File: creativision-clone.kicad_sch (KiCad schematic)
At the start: 0 parts

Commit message: ROM wired up
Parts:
- added C1: 1µF, symbol Device:C_Small
- added JP1, JP2, JP3, JP4: SolderJumper_2_Bridged, symbol Jumper:SolderJumper_2_Bridged
- added R1: 3.3kΩ, symbol Device:R_Small_US
- added R66: 47kΩ, symbol Device:R_Small_US
- added SW1: Reset, symbol Switch:SW_Push
- added U1: 6821, Package_DIP:DIP-40_W15.24mm, symbol Interface:6821
- added U2: SN76489AN, symbol LeakoChips:SN76489AN
- added U3: 6502, Package_DIP:DIP-40_W15.24mm, symbol 65xx:6502
- added U4: TMS9918A, Housings_DIP:DIP-40_W15.24mm_Socket_LongPads, symbol LeakoChips:TMS9918A
- added U5: 27256, Package_DIP:DIP-28_W15.24mm, symbol Memory_EPROM:27256
- added X1: 2MHz, Oscillator:Oscillator_DIP-8, symbol Oscillator:CXO_DIP8
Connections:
- new net: R1.2, SW1.2, U3.6 (~{NMI})
- new net: JP2.2 (B), U5.2 (A12)
- new net: JP1.2 (B), U5.23 (A11)
- new net: JP3.2 (B), U5.26 (A13)
- new net: JP4.2 (B), U5.27 (A14)
- new net +5V: R1.1, R66.1, U3.8 (VCC), U5.28 (VCC), X1.1 (EN), X1.8 (Vcc)
- new net CPUCLK: U3.37 (ϕ0), X1.5 (OUT)
- new net GND: C1.2, JP1.1 (A), JP2.1 (A), JP3.1 (A), JP4.1 (A), SW1.1, U3.1 (VSS), U3.21 (VSS), U5.1 (VPP), U5.14 (GND), X1.4 (GND)
- new net a0: U5.10 (A0)
- new net a1: U5.9 (A1)
- new net a10: U5.21 (A10)
- new net a2: U5.8 (A2)
- new net a3: U5.7 (A3)
- new net a4: U5.6 (A4)
- new net a5: U5.5 (A5)
- new net a6: U5.4 (A6)
- new net a7: U5.3 (A7)
- new net a8: U5.25 (A8)
- new net a9: U5.24 (A9)
- new net d0: U3.33 (D0), U5.11 (D0)
- new net d1: U3.32 (D1), U5.12 (D1)
- new net d2: U3.31 (D2), U5.13 (D2)
- new net d3: U3.30 (D3), U5.15 (D3)
- new net d4: U3.29 (D4), U5.16 (D4)
- new net d5: U3.28 (D5), U5.17 (D5)
- new net d6: U3.27 (D6), U5.18 (D6)
- new net d7: U3.26 (D7), U5.19 (D7)
- new net ~{RESET}: C1.1, R66.2, U3.40 (~{RES})
- new net ~{ROM_RD}: U5.20 (~{CE}), U5.22 (~{OE})
- no-connect marks 0 -> 4
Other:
- note added: "TODO: 9918 interrupt"
- note added: "TODO: 9918 w/r drive"
- note added: "TODO: Which project is it that I had the dual footprint oscillator in?"
- note added: "TODO: are there alternative roms we might want to run?"

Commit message: Work RAM
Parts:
- added R14: 1kΩ, symbol Device:R_Small_US
- added U15: 74LS139, symbol 74xx:74LS139
- added U6: AS6C62256-DIP, Housings_DIP:DIP-28_W15.24mm_Socket_LongPads, symbol AS6C62256:AS6C62256-DIP
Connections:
- net +5V: now also U15.16 (VCC), U6.28 (Vcc)
- net GND: now also U15.15 (E), U15.8 (GND)
- net d0: now also U6.11 (DQ0)
- net d1: now also U6.12 (DQ1)
- net d2: now also U6.13 (DQ2)
- net d3: now also U6.15 (DQ3)
- net d4: now also U6.16 (DQ4)
- net d5: now also U6.17 (DQ5)
- net d6: now also U6.18 (DQ6)
- net d7: now also U6.19 (DQ7)
- new net: R14.2, U6.20 (~{CE})
- new net: U15.1 (E), U15.12 (O0)
- new net: R14.1, U15.4 (O0)
- new net a12: U15.2 (A0)
- new net a13: U15.3 (A1)
- new net a14: U15.14 (A0)
- new net a15: U15.13 (A1)
- new net ~{PIA}: U15.5 (O1)
- new net ~{ROM0}: U15.9 (O3)
- new net ~{ROM1}: U15.10 (O2)
- new net ~{ROM2}: U15.11 (O1)
- new net ~{VDP_R}: U15.6 (O2)
- new net ~{VDP_W}: U15.7 (O3)
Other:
- note added: "BIOS ROM"
- note added: "Main System RAM"
- note added: "TODO: Connector P1?"
- note added: "TODO: R/W W/R signals"

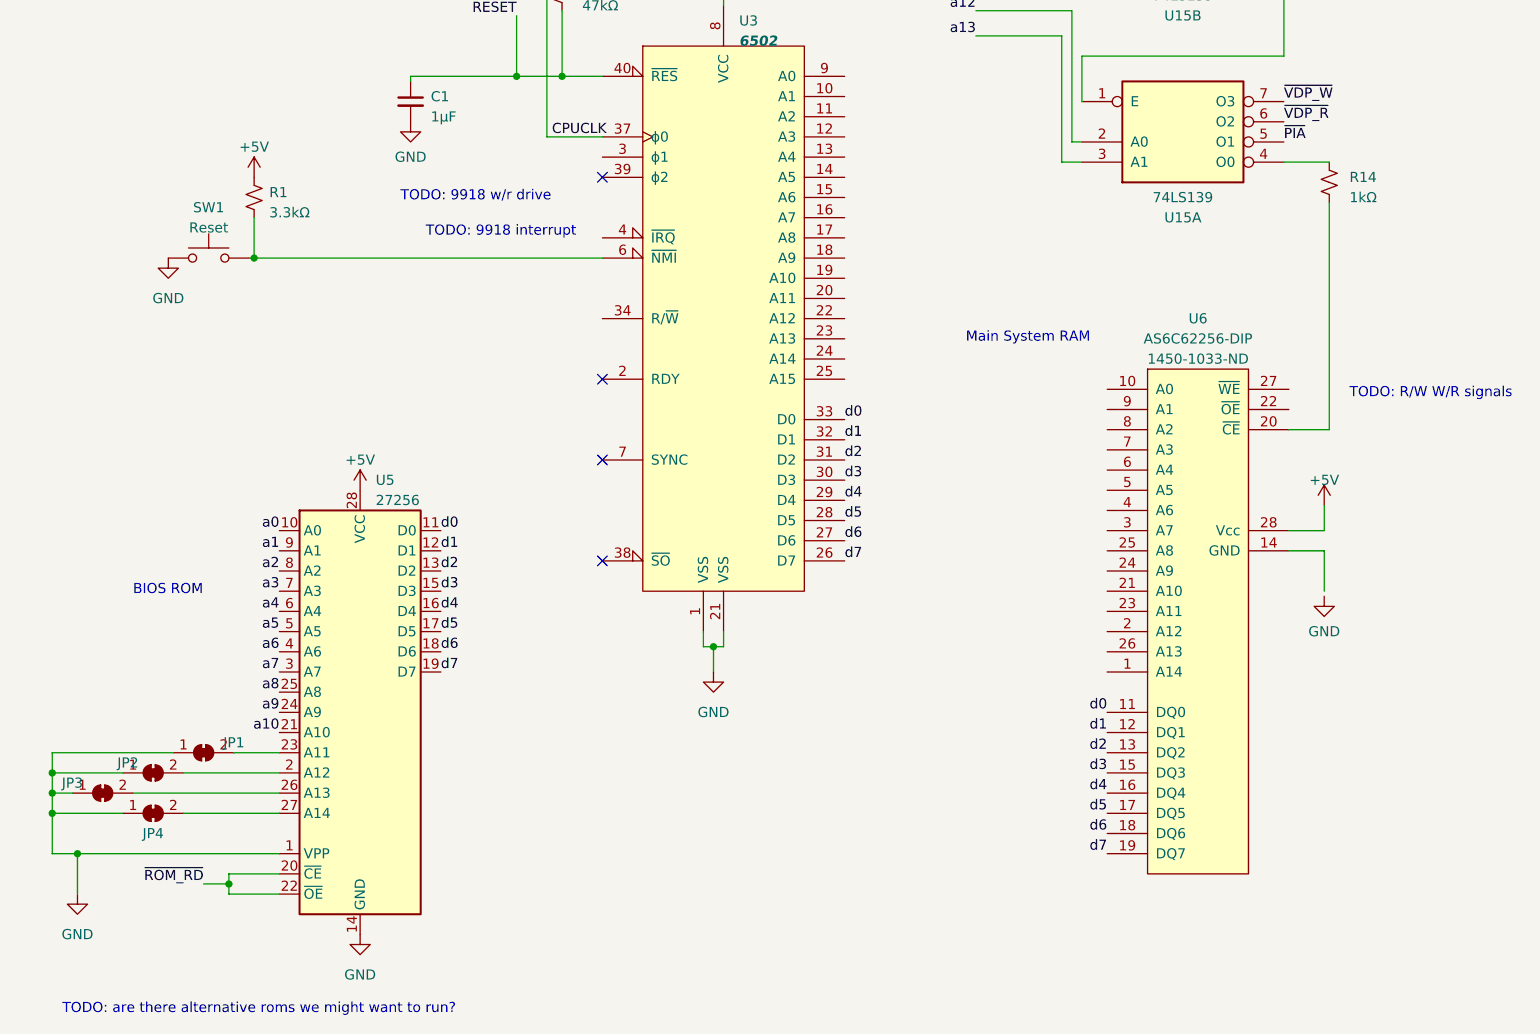
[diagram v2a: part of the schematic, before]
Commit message: Decody.py for 139 config
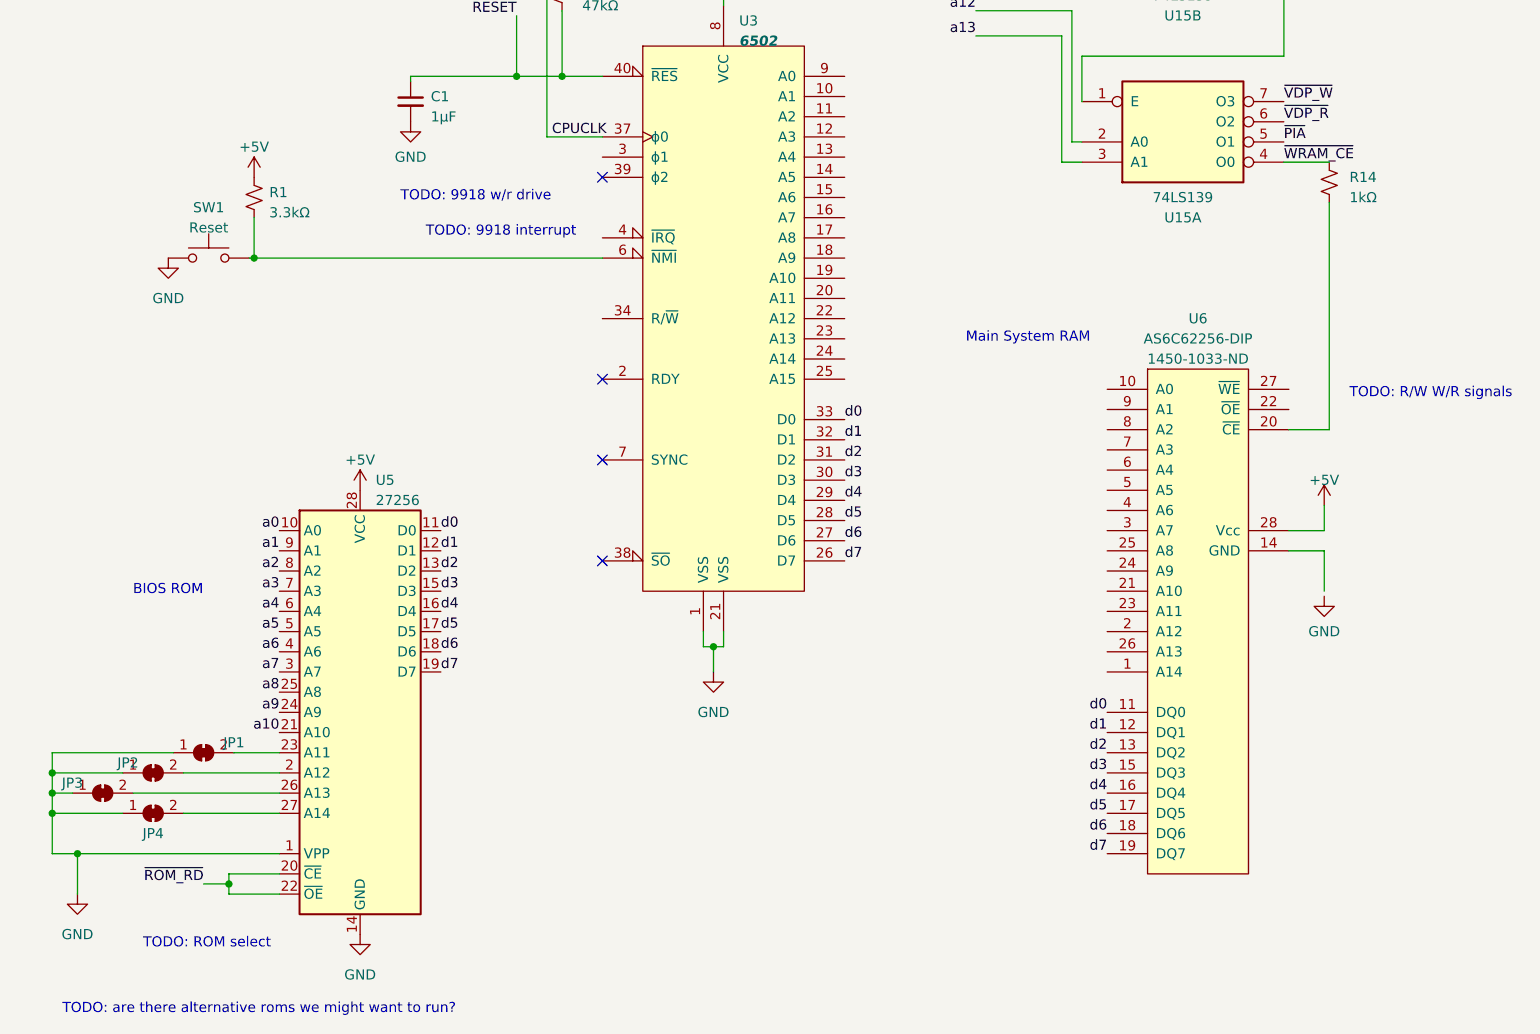
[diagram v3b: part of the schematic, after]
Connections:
- net ~{WRAM_CE}: now reaches R14.1, U15.4 (O0)
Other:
- note added: "TODO: ROM select"
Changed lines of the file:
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@@
+    (effects (font (size 1.27 1.27)) (justify left bottom))
+  )
+  (text "TODO: ROM select" (at 24.765 178.435 0)
     (effects (font (size 1.27 1.27)) (justify left bottom))
   )
@@
     (effects (font (size 1.27 1.27)) (justify left bottom))
   )
+  (label "~{WRAM_CE}" (at 168.275 79.375 0) (fields_autoplaced)
+    (effects (font (size 1.27 1.27)) (justify left bottom))
+  )

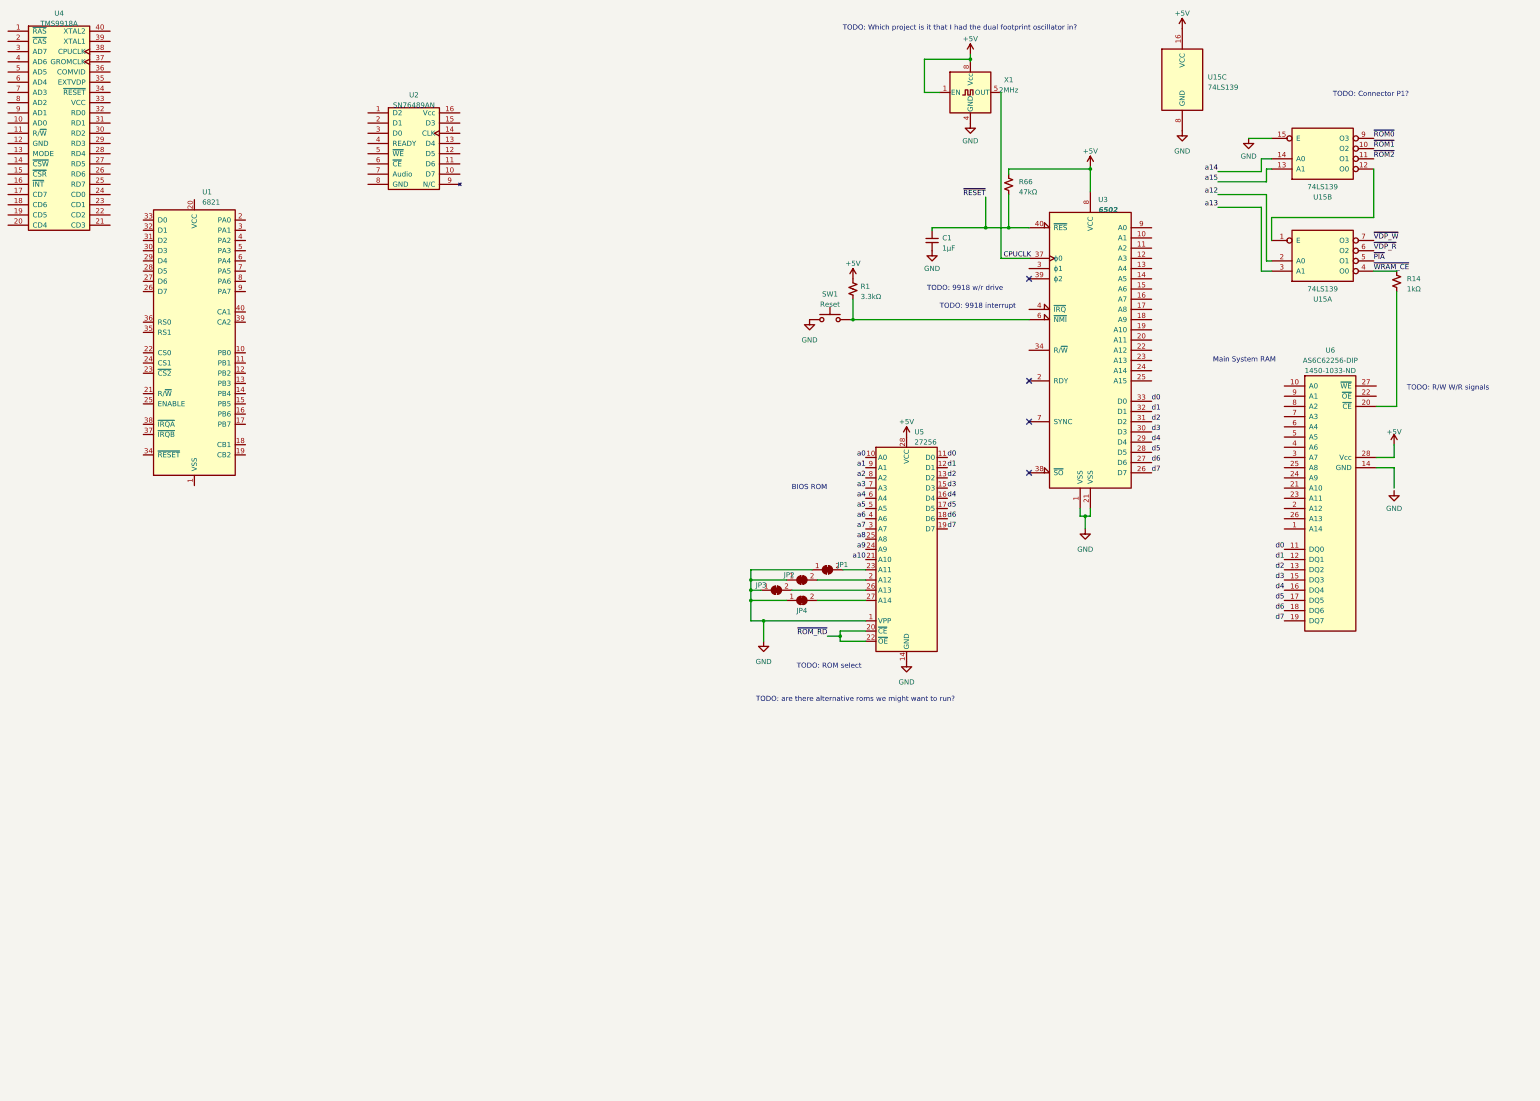
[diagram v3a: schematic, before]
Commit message: 6502A wired up
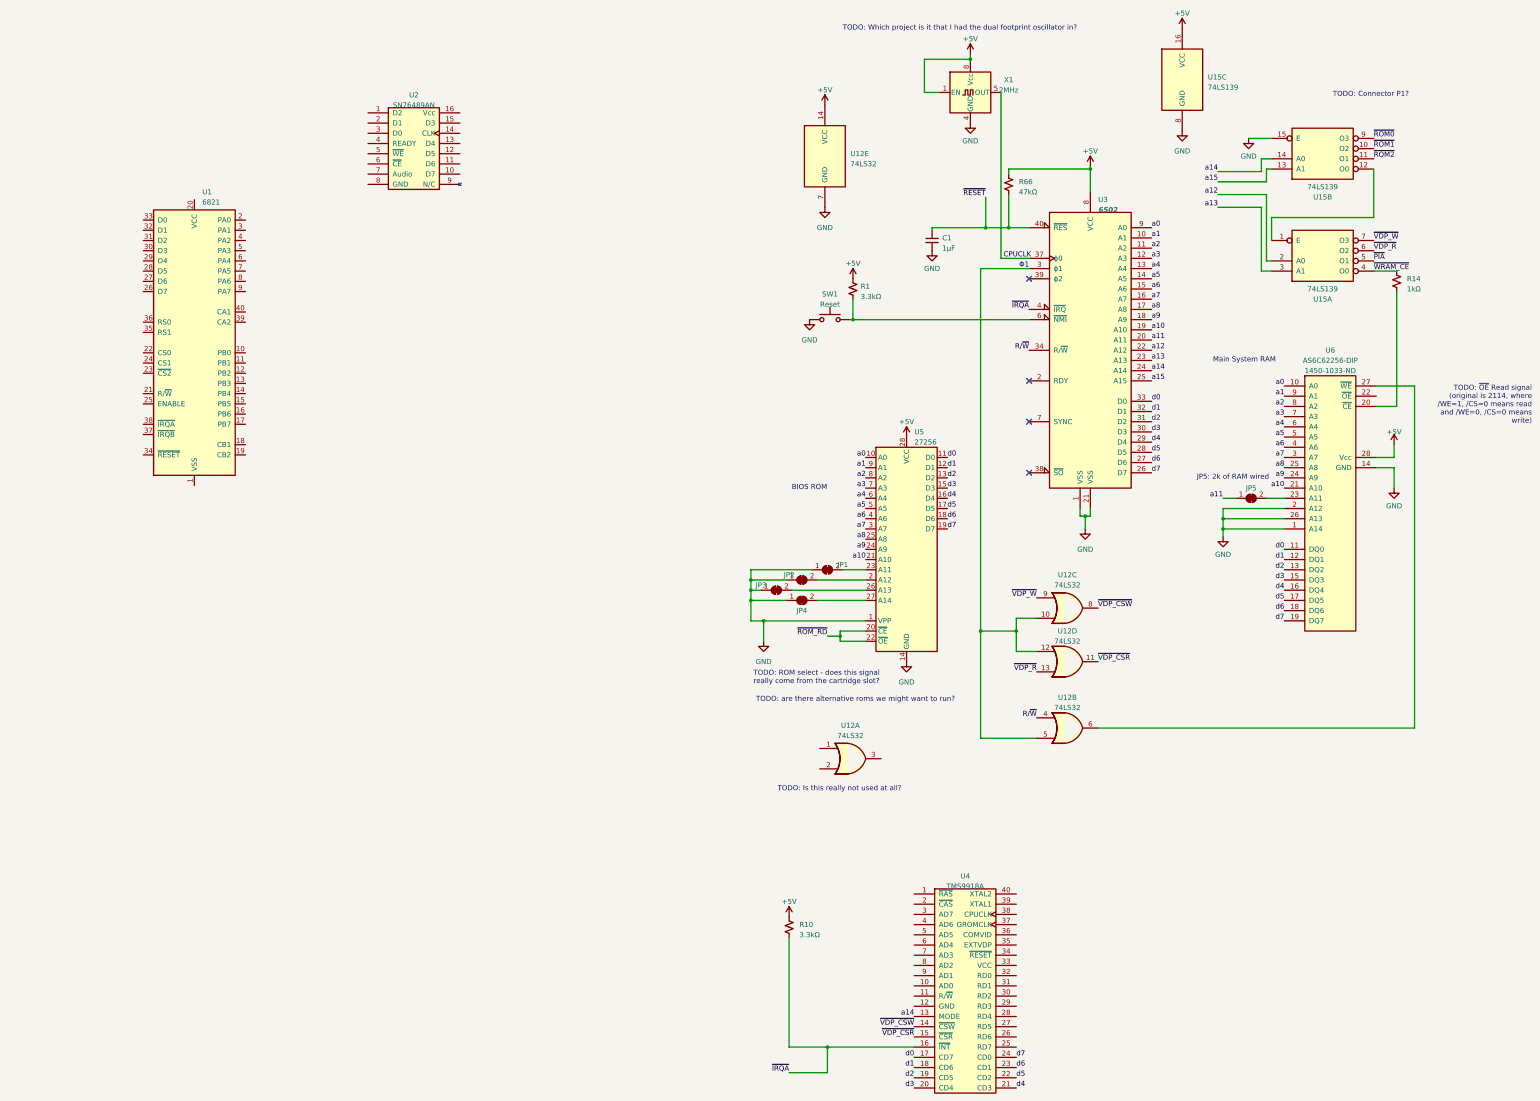
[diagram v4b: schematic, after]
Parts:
- added JP5: SolderJumper_2_Bridged, symbol Jumper:SolderJumper_2_Bridged
- added R10: 3.3kΩ, symbol Device:R_Small_US
- added U12: 74LS32, symbol 74xx:74LS32
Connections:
- net +5V: now also R10.1, U12.14 (VCC)
- net GND: now also U6.1 (A14), U6.14 (GND), U6.2 (A12), U6.26 (A13), U12.7 (GND)
- net a0: now also U3.9 (A0), U6.10 (A0)
- net a1: now also U3.10 (A1), U6.9 (A1)
- net a10: now also U3.19 (A10), U6.21 (A10)
- net a12: now also U3.22 (A12)
- net a13: now also U3.23 (A13)
- net a14: now also U3.24 (A14), U4.13 (MODE)
- net a15: now also U3.25 (A15)
- net a2: now also U3.11 (A2), U6.8 (A2)
- net a3: now also U3.12 (A3), U6.7 (A3)
- net a4: now also U3.13 (A4), U6.6 (A4)
- net a5: now also U3.14 (A5), U6.5 (A5)
- net a6: now also U3.15 (A6), U6.4 (A6)
- net a7: now also U3.16 (A7), U6.3 (A7)
- net a8: now also U3.17 (A8), U6.25 (A8)
- net a9: now also U3.18 (A9), U6.24 (A9)
- net d0: now also U4.17 (CD7)
- net d1: now also U4.18 (CD6)
- net d2: now also U4.19 (CD5)
- net d3: now also U4.20 (CD4)
- net d4: now also U4.21 (CD3)
- net d5: now also U4.22 (CD2)
- net d6: now also U4.23 (CD1)
- net d7: now also U4.24 (CD0)
- net ~{VDP_R}: now also U12.13
- net ~{VDP_W}: now also U12.9
- net a11: now reaches U3.20 (A11)
- net a11: now also JP5.1 (A)
- net Φ1: now reaches U3.3 (ϕ1)
- net Φ1: now also U12.10, U12.12, U12.5
- net R/~{W}: now reaches U3.34 (R/~{W})
- net R/~{W}: now also U12.4
- net ~{IRQA}: now reaches U3.4 (~{IRQ})
- net ~{IRQA}: now also U4.16 (~{INT}), R10.2
- net at U6.23 (A11): now also JP5.2 (B)
- net at U6.27 (~{WE}): now also U12.6
- net ~{VDP_CSW}: now reaches U4.14 (~{CSW})
- net ~{VDP_CSW}: now also U12.8
- net ~{VDP_CSR}: now reaches U4.15 (~{CSR})
- net ~{VDP_CSR}: now also U12.11
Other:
- note added: "JP5: 2k of RAM wired"
- note added: "TODO: Is this really not used at all?"
- note added: "TODO: ROM select - does this signal really come from the cartridge slot?"
- note added: "TODO: ~{OE} Read signal (original is 2114, where /WE=1, /CS=0 means read and /WE=0, /CS=0 means write)"
- note removed: "TODO: 9918 interrupt"
- note removed: "TODO: 9918 w/r drive"
- note removed: "TODO: R/W W/R signals"
- note removed: "TODO: ROM select"
- moved on the sheet: U4
